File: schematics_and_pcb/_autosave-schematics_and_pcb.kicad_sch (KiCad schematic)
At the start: 58 parts, among them J1 RND 205-00623, J2 RND 205-00627, J3 Motor con, J5 Conn_01x04_Male, J6 USB_OTG_custom, Q1 PMV213SN, SW1 RND 210-00210, U1 LP2985IM5-2.0/NOPB, U2 TS3480CX33 RFG, U3 PWM3389DM-T3QU, U4 STM32F401RBTx, Y1 YLFXTAL029370

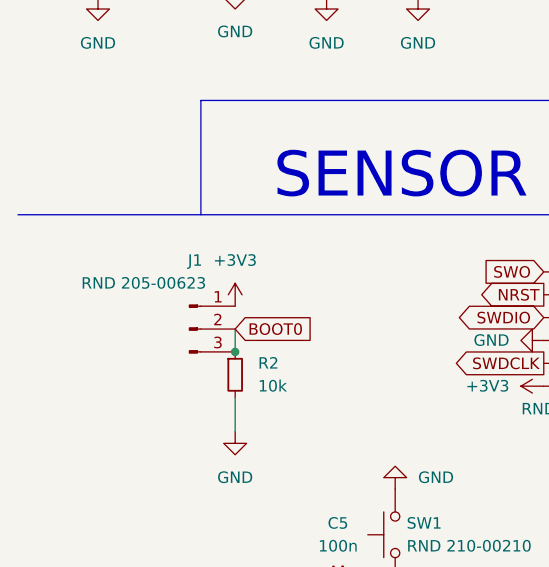
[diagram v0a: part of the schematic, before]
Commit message: fixed some of the routing
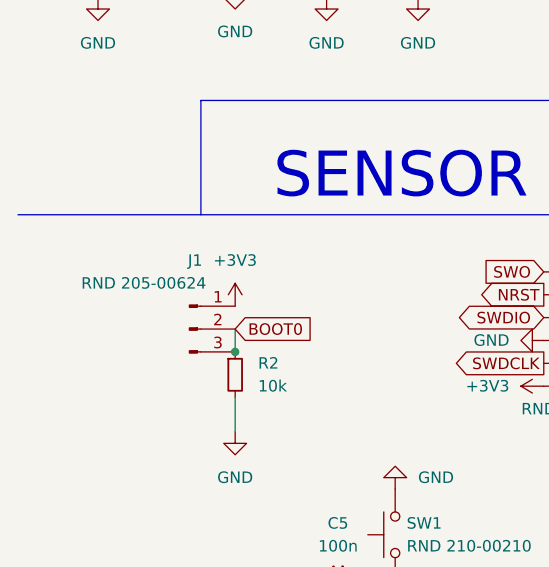
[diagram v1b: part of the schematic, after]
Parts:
- J1: value RND 205-00623 -> RND 205-00624
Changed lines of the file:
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@@
     (in_bom yes) (on_board yes)
     (property "Reference" "J1" (id 0) (at 32.385 142.24 0))
-    (property "Value" "RND 205-00623 " (id 1) (at 26.67 144.78 0))
+    (property "Value" "RND 205-00624" (id 1) (at 26.67 144.78 0))
     (property "Footprint" "Connector_PinHeader_2.54mm:PinHeader_1x03_P2.54mm_Vertical" (id 2) (at 31.75 149.86 0)
       (effects (font (size 1.27 1.27)) hide)
@@
     )
     (path "/99d62c77-db75-4888-85e2-73a6b151a621"
-      (reference "J1") (unit 1) (value "RND 205-00623 ") (footprint "Connector_PinHeader_2.54mm:PinHeader_1x03_P2.54mm_Vertical")
+      (reference "J1") (unit 1) (value "RND 205-00624") (footprint "Connector_PinHeader_2.54mm:PinHeader_1x03_P2.54mm_Vertical")
     )
     (path "/5f79ca16-1b5e-47ab-90c2-75b897302cd0"
